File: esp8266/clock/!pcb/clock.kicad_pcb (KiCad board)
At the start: 2 copper layers, 45.2 x 57 mm, 17 parts, among them J1 GPIO, U3 BME280, U4 OLED, U5 LED, U6 SPARE

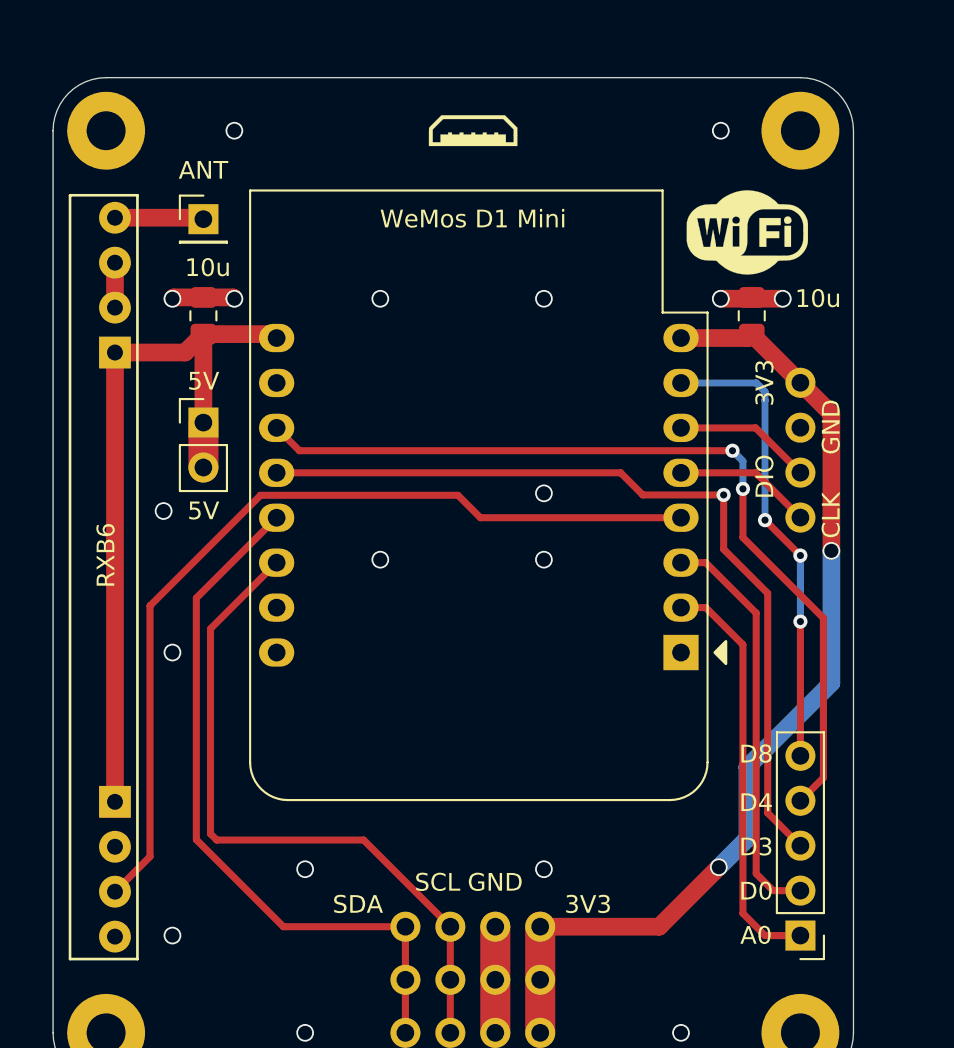
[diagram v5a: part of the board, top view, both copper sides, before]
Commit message: clock: Send v10 to fab
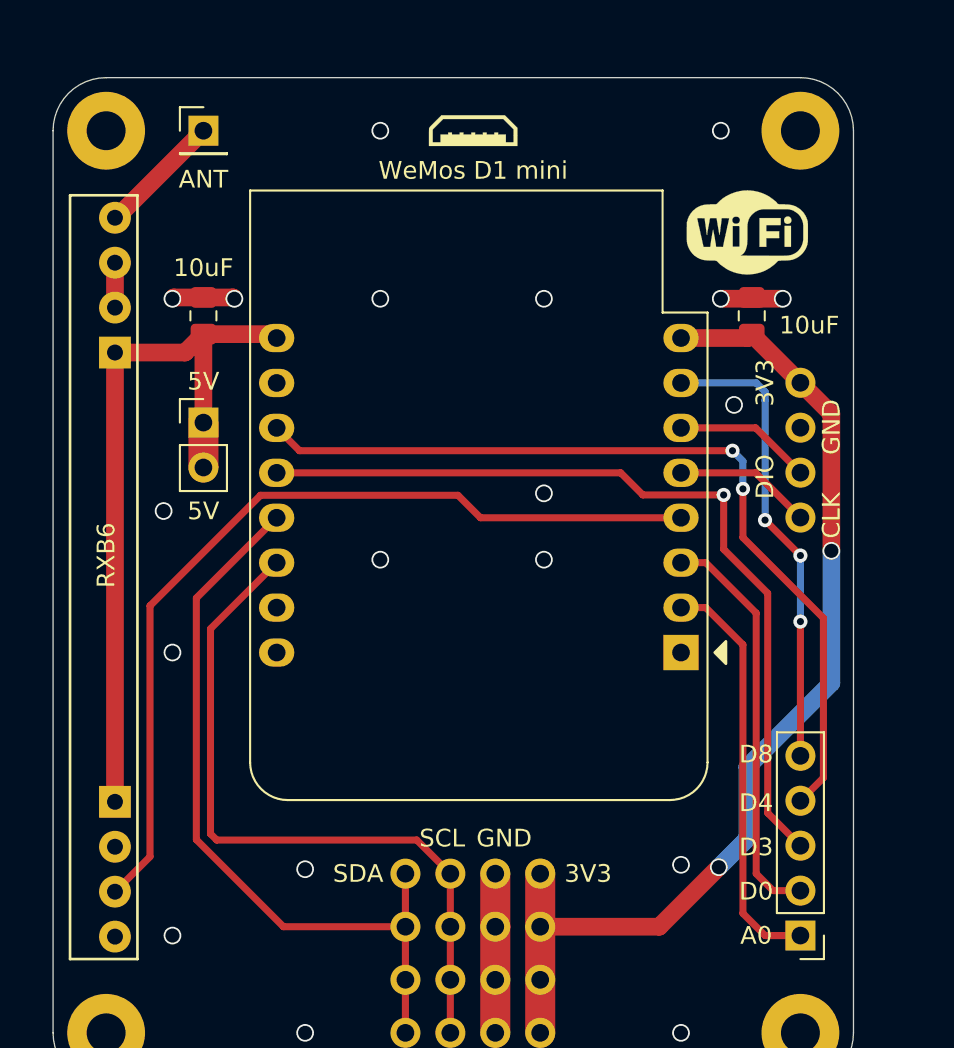
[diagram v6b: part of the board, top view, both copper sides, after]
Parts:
- added U7: SPARE2, !myfoots:4pinI2C, F.Cu at (74.2, 106.0)
- WeMos D1 mini: renamed from WeMos D1 Mini
- moved ANT 5.00 mm to (59.0, 64.0)
- renumbered 10u to 10uF
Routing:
- net GND: track 15.6 -> 18.6 mm, vias 18 -> 19
- net SDA: track 39.9 -> 42.9 mm
- net +3V3: track 56.2 -> 59.2 mm
- net ANT: track 5.03 -> 7.37 mm
- net SCL: track 38.6 -> 40.4 mm
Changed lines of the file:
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@@
     (thickness 1.6)
     (drawings 23)
-    (tracks 112)
+    (tracks 118)
     (zones 0)
-    (modules 17)
+    (modules 18)
     (nets 19)
   )
@@
     (tags "capacitor handsolder")
     (attr smd)
-    (fp_text reference 10u (at 2.7125 0.25 180) (layer F.SilkS)
+    (fp_text reference 10uF (at 2.7125 0 180) (layer F.SilkS)
       (effects (font (size 1 1) (thickness 0.15)))
     )
@@
     (tags "capacitor handsolder")
     (attr smd)
-    (fp_text reference 10u (at -0.9625 -3.75 180) (layer F.SilkS)
+    (fp_text reference 10uF (at 0.5375 -3.25 180) (layer F.SilkS)
       (effects (font (size 1 1) (thickness 0.15)))
     )
@@
   )
   (module Connector_PinHeader_2.54mm:PinHeader_1x01_P2.54mm_Vertical (layer F.Cu)
-    (at 59 69)
+    (at 59 64)
     (descr "Through hole straight pin header, 1x01, 2.54mm pitch, single row")
     (tags "Through hole pin header THT 1x01 2.54mm single row")
-    (fp_text reference ANT (at 0 -2.75) (layer F.SilkS)
+    (fp_text reference ANT (at 0 2.75) (layer F.SilkS)
       (effects (font (size 1 1) (thickness 0.15)))
     )
@@
     (descr "16-pin module, column spacing 22.86 mm (900 mils), https://wiki.wemos.cc/products:d1:d1_mini, https://c1.staticflickr.com/1/734/31400410271_f278b087db_z.jpg")
     (tags "ESP8266 WiFi microcontroller")
-    (fp_text reference "WeMos D1 Mini" (at 11.75 24.5) (layer F.SilkS)
+    (fp_text reference "WeMos D1 mini" (at 11.75 27.25) (layer F.SilkS)
       (effects (font (size 1 1) (thickness 0.15)))
     )
@@
       (effects (font (size 1 1) (thickness 0.15)))
     )
-    (fp_text user 3V3 (at 6.52 -1.25) (layer F.SilkS)
+    (fp_text user 3V3 (at 6.52 -3) (layer F.SilkS)
       (effects (font (size 1 1) (thickness 0.15)))
     )
@@
       (effects (font (size 1 1) (thickness 0.15)))
     )
-    (fp_text user SDA (at -6.5 -1.25) (layer F.SilkS)
+    (fp_text user SDA (at -6.48 -3) (layer F.SilkS)
       (effects (font (size 1 1) (thickness 0.15)))
     )
@@
       (effects (font (size 1 1) (thickness 0.15)))
     )
-    (fp_text user GND (at 1.27 -8.5) (layer F.SilkS)
+    (fp_text user GND (at 1.27 -8.5) (layer F.Fab)
       (effects (font (size 1 1) (thickness 0.15)))
     )
@@
       (effects (font (size 1 1) (thickness 0.15)))
     )
-    (fp_text user SCL (at -2 -8.5) (layer F.SilkS)
+    (fp_text user SCL (at -2 -8.5) (layer F.Fab)
       (effects (font (size 1 1) (thickness 0.15)))
     )
@@
       (rotate (xyz 0 0 0))
     )
+  )
+  (module !myfoots:4pinI2C (layer F.Cu)
+    (at 74.23 106)
+    (fp_text reference U7 (at 0 7.62) (layer F.Fab)
+      (effects (font (size 1 1) (thickness 0.15)))
+    )
+    (fp_text value SPARE2 (at 0 5.08) (layer F.Fab)
+      (effects (font (size 1 1) (thickness 0.15)))
+    )
+    (fp_text user VIN (at 6.35 0) (layer F.Fab)
+      (effects (font (size 1 1) (thickness 0.15)))
+    )
+    (fp_text user GND (at 1.77 -2) (layer F.SilkS)
+      (effects (font (size 1 1) (thickness 0.15)))
+    )
+    (fp_text user SDA (at -6.5 0) (layer F.Fab)
+      (effects (font (size 1 1) (thickness 0.15)))
+    )
+    (fp_text user SCL (at -1.73 -2) (layer F.SilkS)
+      (effects (font (size 1 1) (thickness 0.15)))
+    )
+    (pad 4 thru_hole circle (at -3.81 0) (size 1.7 1.7) (drill 1) (layers *.Cu *.Mask)
+      (net 13 SDA))
+    (pad 3 thru_hole circle (at -1.27 0) (size 1.7 1.7) (drill 1) (layers *.Cu *.Mask)
+      (net 14 SCL))
+    (pad 2 thru_hole circle (at 1.27 0) (size 1.7 1.7) (drill 1) (layers *.Cu *.Mask)
+      (net 2 GND))
+    (pad 1 thru_hole circle (at 3.81 0 90) (size 1.7 1.7) (drill 1) (layers *.Cu *.Mask)
+      (net 3 +3V3))
   )
   (dimension 51 (width 0.15) (layer Eco2.User)
@@
   (via (at 64.75 105.75) (size 1) (drill 0.8) (layers F.Cu B.Cu) (net 2))
   (segment (start 75.5 109) (end 75.5 115) (width 1.7) (layer F.Cu) (net 2))
-  (via (at 78.25 105.75) (size 1) (drill 0.8) (layers F.Cu B.Cu) (net 2))
   (via (at 64.75 115) (size 1) (drill 0.8) (layers F.Cu B.Cu) (net 2))
   (via (at 86 115) (size 1) (drill 0.8) (layers F.Cu B.Cu) (net 2))
@@
   (via (at 78.25 73.5) (size 1) (drill 0.8) (layers F.Cu B.Cu) (net 2))
   (via (at 69 73.5) (size 1) (drill 0.8) (layers F.Cu B.Cu) (net 2))
-  (via (at 60.75 64) (size 1) (drill 0.8) (layers F.Cu B.Cu) (net 2))
   (via (at 88.25 64) (size 1) (drill 0.8) (layers F.Cu B.Cu) (net 2))
   (via (at 57.25 93.5) (size 1) (drill 0.8) (layers F.Cu B.Cu) (net 2))
@@
   (via (at 57.25 109.5) (size 1) (drill 0.8) (layers F.Cu B.Cu) (net 2))
   (segment (start 54 71.46) (end 54 74) (width 1) (layer F.Cu) (net 2))
+  (segment (start 75.5 106) (end 75.5 109) (width 1.7) (layer F.Cu) (net 2))
+  (via (at 86 105.5) (size 1) (drill 0.8) (layers F.Cu B.Cu) (net 2))
+  (via (at 89 79.5) (size 1) (drill 0.8) (layers F.Cu B.Cu) (net 2))
+  (via (at 69 64) (size 1) (drill 0.8) (layers F.Cu B.Cu) (net 2))
   (segment (start 84.772808 109) (end 78.04 109) (width 1) (layer F.Cu) (net 3))
   (segment (start 94.500001 80.000001) (end 94.500001 87.749999) (width 1) (layer F.Cu) (net 3))
@@
   (segment (start 94.500001 87.749999) (end 94.500001 95.221997) (width 1) (layer B.Cu) (net 3))
   (segment (start 78.04 109) (end 78.04 115) (width 1.7) (layer F.Cu) (net 3))
+  (segment (start 78.04 106) (end 78.04 109) (width 1.7) (layer F.Cu) (net 3))
   (segment (start 87.4 90.96) (end 89.5 93.06) (width 0.4) (layer F.Cu) (net 4))
   (segment (start 86 90.96) (end 87.4 90.96) (width 0.4) (layer F.Cu) (net 4))
@@
   (via (at 92.75 91.75) (size 0.8) (drill 0.4) (layers F.Cu B.Cu) (net 8))
   (segment (start 92.75 88.016002) (end 92.75 91.75) (width 0.4) (layer B.Cu) (net 8))
-  (segment (start 58.92 68.92) (end 59 69) (width 1) (layer F.Cu) (net 9))
-  (segment (start 54 68.92) (end 58.92 68.92) (width 1) (layer F.Cu) (net 9))
+  (segment (start 54 68.92) (end 54.33 68.92) (width 1) (layer F.Cu) (net 9))
+  (segment (start 54.08 68.92) (end 59 64) (width 1) (layer F.Cu) (net 9))
+  (segment (start 54 68.92) (end 54.08 68.92) (width 1) (layer F.Cu) (net 9))
   (segment (start 55.98 105.04) (end 55.98 90.860087) (width 0.4) (layer F.Cu) (net 10))
   (segment (start 54 107.02) (end 55.98 105.04) (width 0.4) (layer F.Cu) (net 10))
@@
   (segment (start 70.42 109) (end 63.520072 109) (width 0.4) (layer F.Cu) (net 13))
   (segment (start 70.42 109) (end 70.42 115) (width 0.4) (layer F.Cu) (net 13))
-  (segment (start 59.39999 92.16001) (end 63.14 88.42) (width 0.4) (layer F.Cu) (net 14))
-  (segment (start 59.751466 104.10001) (end 59.39999 103.748534) (width 0.4) (layer F.Cu) (net 14))
-  (segment (start 68.06001 104.10001) (end 59.751466 104.10001) (width 0.4) (layer F.Cu) (net 14))
-  (segment (start 59.39999 103.748534) (end 59.39999 92.16001) (width 0.4) (layer F.Cu) (net 14))
-  (segment (start 72.96 109) (end 68.06001 104.10001) (width 0.4) (layer F.Cu) (net 14))
+  (segment (start 70.42 109) (end 70.42 106) (width 0.4) (layer F.Cu) (net 13))
   (segment (start 72.96 109) (end 72.96 115) (width 0.4) (layer F.Cu) (net 14))
+  (segment (start 71.06001 104.10001) (end 72.96 106) (width 0.4) (layer F.Cu) (net 14))
+  (segment (start 59.751466 104.10001) (end 71.06001 104.10001) (width 0.4) (layer F.Cu) (net 14))
+  (segment (start 59.39999 103.748534) (end 59.751466 104.10001) (width 0.4) (layer F.Cu) (net 14))
+  (segment (start 59.39999 92.16001) (end 59.39999 103.748534) (width 0.4) (layer F.Cu) (net 14))
+  (segment (start 63.14 88.42) (end 59.39999 92.16001) (width 0.4) (layer F.Cu) (net 14))
+  (segment (start 72.96 106) (end 72.96 109) (width 0.4) (layer F.Cu) (net 14))
   (zone (net 2) (net_name GND) (layer F.Cu) (hatch edge 0.508)
     (connect_pads (clearance 0.508))
